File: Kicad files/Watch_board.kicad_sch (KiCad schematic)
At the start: 60 parts, among them J1 USB_C_Receptacle_USB2.0, J2 MOT1, J3 MOT2, Q1 BC846, SW2 BTN_L, SW3 BTN_R, U1 LTC3531, U2 MAX1811, U3 BMP280, U4 DS3231MZ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

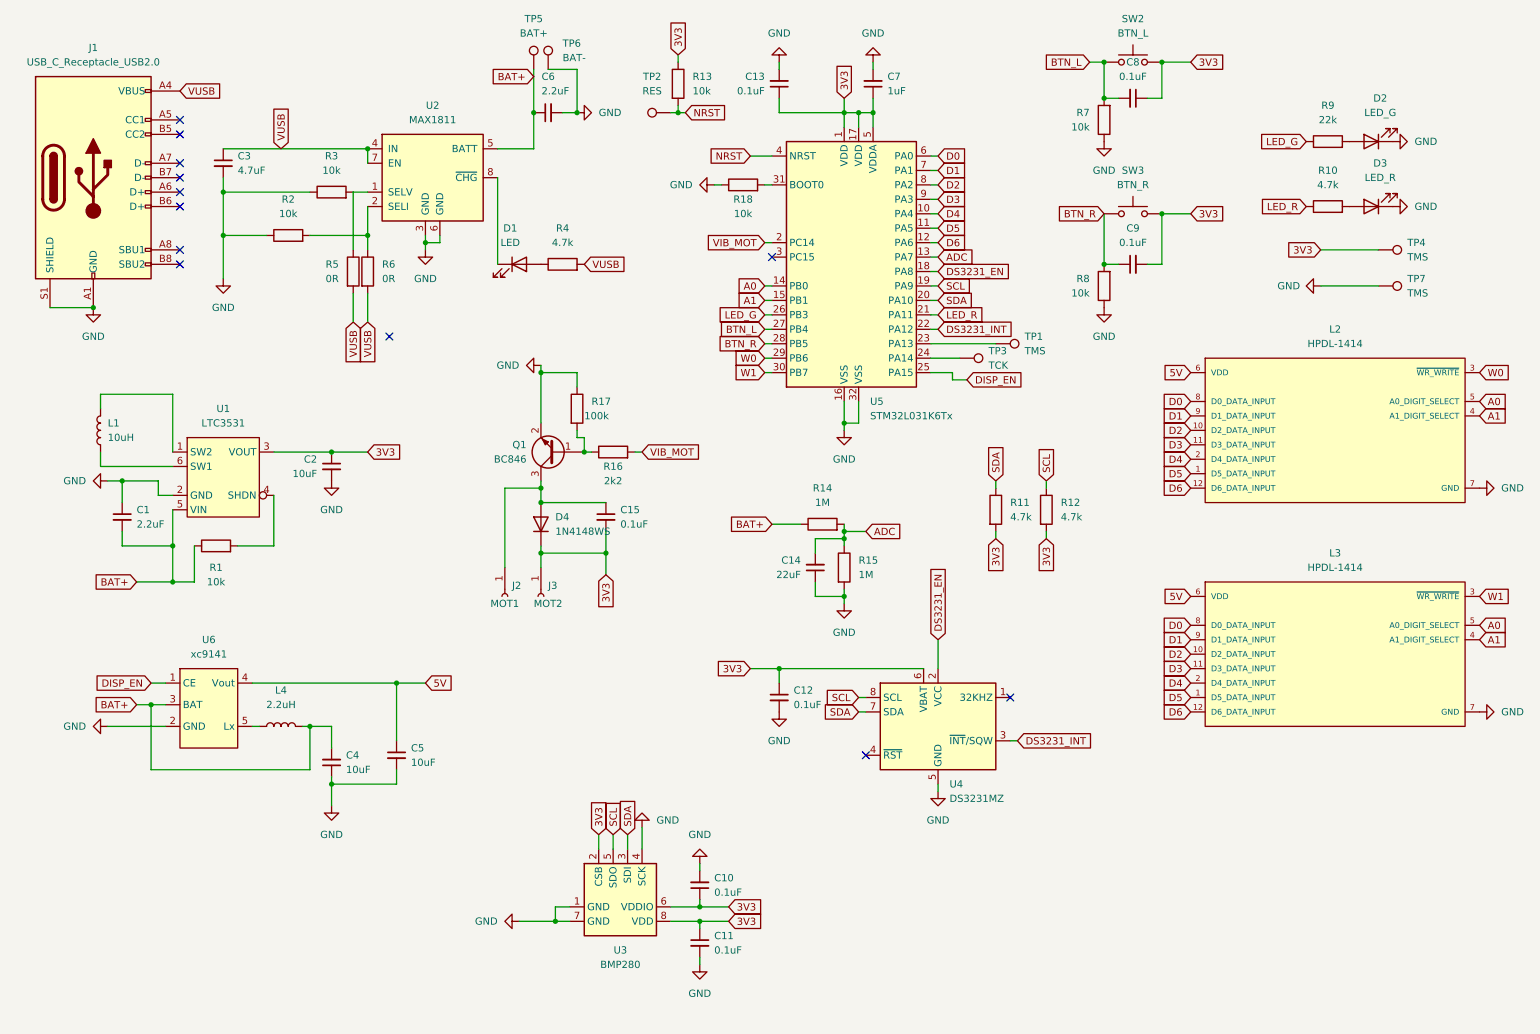
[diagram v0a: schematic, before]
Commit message: updated to HCMS-2904 (WIP)
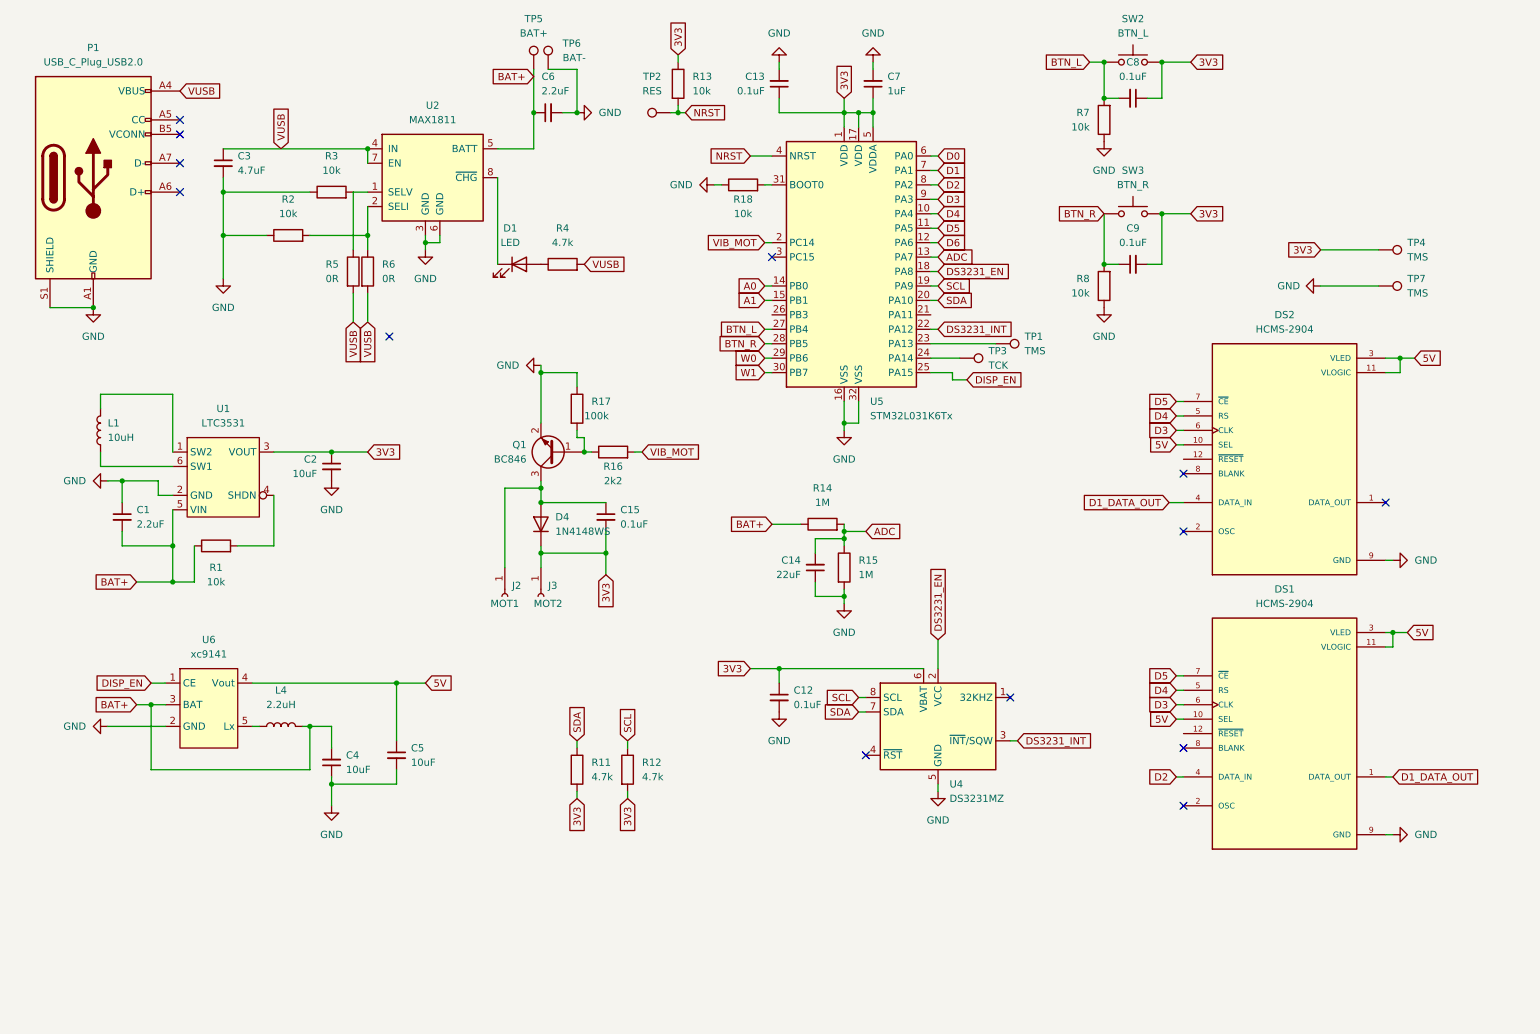
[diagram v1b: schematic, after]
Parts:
- removed C10, C11: 0.1uF, Capacitor_SMD:C_0603_1608Metric_Pad1.08x0.95mm_HandSolder, symbol Device:C_Small
- removed D2: LED_G, LED_SMD:LED_1206_3216Metric_Pad1.42x1.75mm_HandSolder, symbol Device:LED
- removed D3: LED_R, LED_SMD:LED_1206_3216Metric_Pad1.42x1.75mm_HandSolder, symbol Device:LED
- removed J1: USB_C_Receptacle_USB2.0, USB-C-Connectors:TYPE-C-31-M-17_handsolder, symbol Connector:USB_C_Receptacle_USB2.0
- removed L2, L3: HPDL-1414, eec:Broadcom-HPDL-1414-0, symbol eec:HPDL-1414
- removed R10: 4.7k, Resistor_SMD:R_0603_1608Metric_Pad0.98x0.95mm_HandSolder, symbol Device:R
- removed R9: 22k, Resistor_SMD:R_0603_1608Metric_Pad0.98x0.95mm_HandSolder, symbol Device:R
- removed U3: BMP280, Package_LGA:Bosch_LGA-8_2x2.5mm_P0.65mm_ClockwisePinNumbering, symbol Sensor_Pressure:BMP280
- added DS1, DS2: HCMS-2904, HCMS-290x:DIPS762W51P254L1778H508Q12, symbol HCMS-2901:HCMS-2901
- added P1: USB_C_Plug_USB2.0, USB-C-Connectors:TYPE-C-31-M-17_handsolder, symbol Connector:USB_C_Plug_USB2.0
- SW2, SW3: footprint Button_Switch_SMD:SW_Push_1P1T_NO_CK_KMR2 -> Button_Switch_SMD:SW_SPST_PTS810
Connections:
- net 5V: now also DS1.10 (SEL), DS1.11 (VLOGIC), DS1.3 (VLED), DS2.10 (SEL), DS2.11 (VLOGIC), DS2.3 (VLED)
- net D2: now also DS1.4 (DATA_IN)
- net D3: now also DS1.6 (CLK), DS2.6 (CLK)
- net D4: now also DS1.5 (RS), DS2.5 (RS)
- net D5: now also DS1.7 (~{CE}), DS2.7 (~{CE})
- net GND: now also DS1.9 (GND), DS2.9 (GND), P1.A1 (GND), P1.A12 (GND), P1.B1 (GND), P1.B12 (GND), P1.S1 (SHIELD)
- net VUSB: now also P1.A4 (VBUS), P1.A9 (VBUS), P1.B4 (VBUS), P1.B9 (VBUS)
- net LED_G: no longer names the net of U5.26 (PB3)
- net LED_R: no longer names the net of U5.21 (PA11)
- new net D1_DATA_OUT: DS1.1 (DATA_OUT), DS2.4 (DATA_IN)
- no-connect marks 12 -> 13
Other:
- moved on the sheet: R11, R12

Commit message: updated kicad schematics to add light sensor, updated code
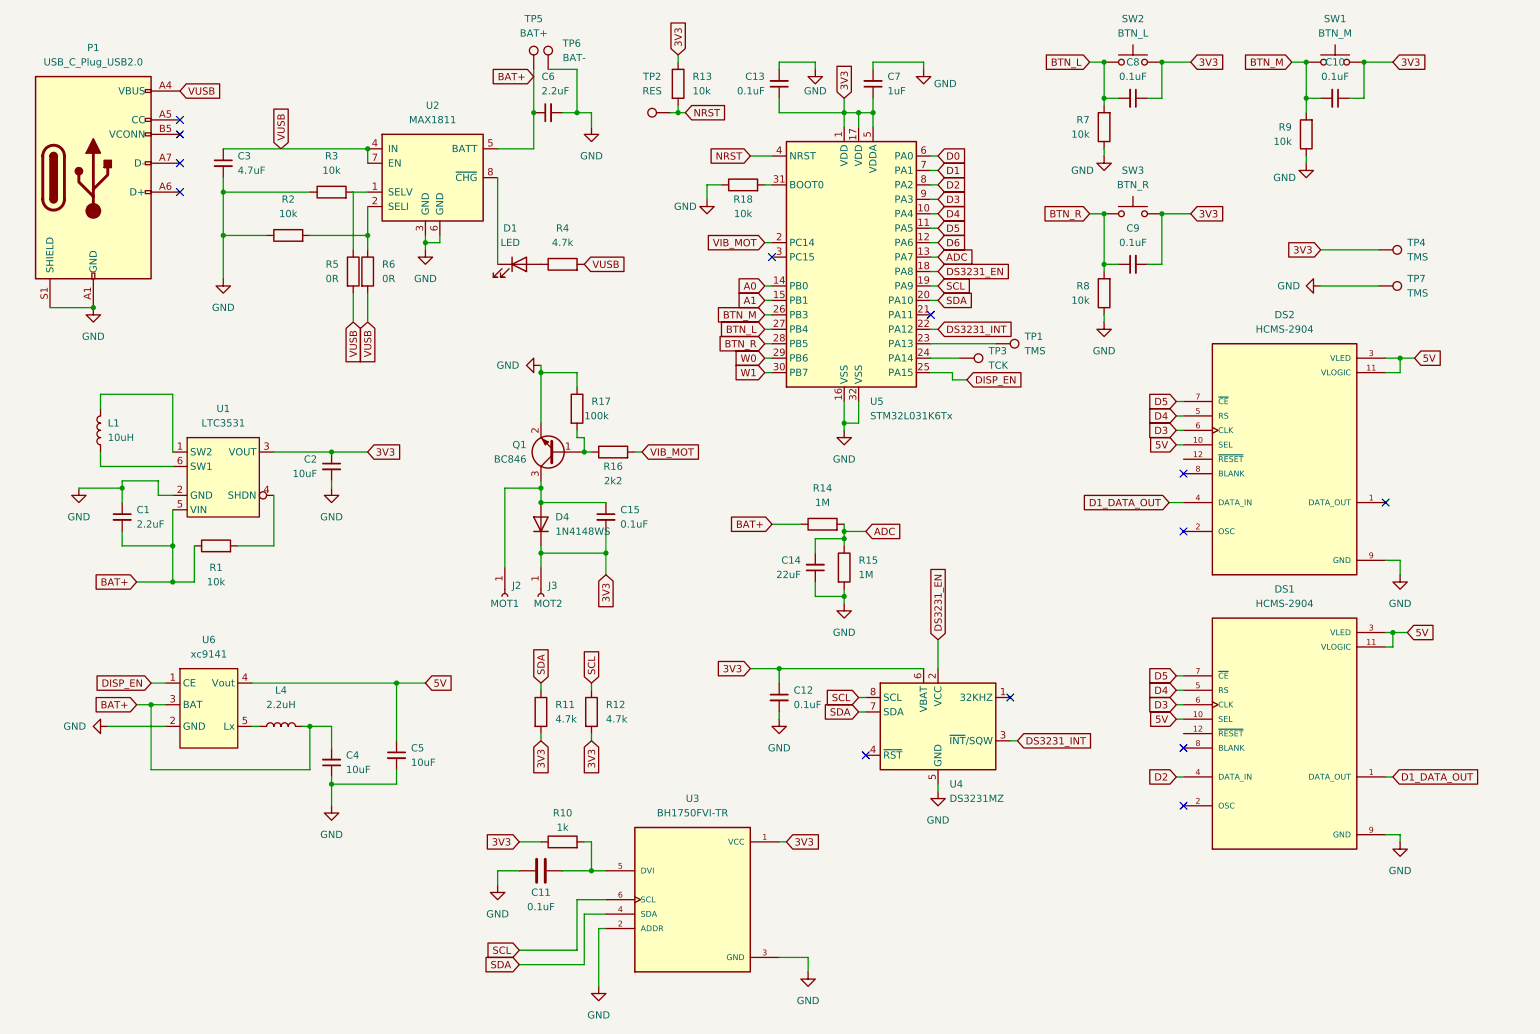
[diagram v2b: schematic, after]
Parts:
- added C10: 0.1uF, Capacitor_SMD:C_0603_1608Metric_Pad1.08x0.95mm_HandSolder, symbol Device:C_Small
- added C11: 0.1uF, Capacitor_SMD:C_0603_1608Metric_Pad1.08x0.95mm_HandSolder, symbol Device:C
- added R10: 1k, Resistor_SMD:R_0603_1608Metric_Pad0.98x0.95mm_HandSolder, symbol Device:R
- added R9: 10k, Resistor_SMD:R_0603_1608Metric_Pad0.98x0.95mm_HandSolder, symbol Device:R
- added SW1: BTN_M, Button_Switch_SMD:SW_SPST_PTS810, symbol Switch:SW_Push
- added U3: BH1750FVI-TR, BH1750FVI-TR:XDCR_BH1750FVI-TR, symbol BH1750FVI-TR:BH1750FVI-TR
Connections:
- net 3V3: now also C10.1, R10.1, SW1.2, U3.1 (VCC)
- net GND: now also C11.1, R9.1, U3.2 (ADDR), U3.3 (GND)
- net SCL: now also U3.6 (SCL)
- net SDA: now also U3.4 (SDA)
- net BTN_M: now reaches U5.26 (PB3)
- net BTN_M: now also C10.2, R9.2, SW1.1
- new net: C11.2, R10.2, U3.5 (DVI)
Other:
- moved on the sheet: R11, R12, R7, R8

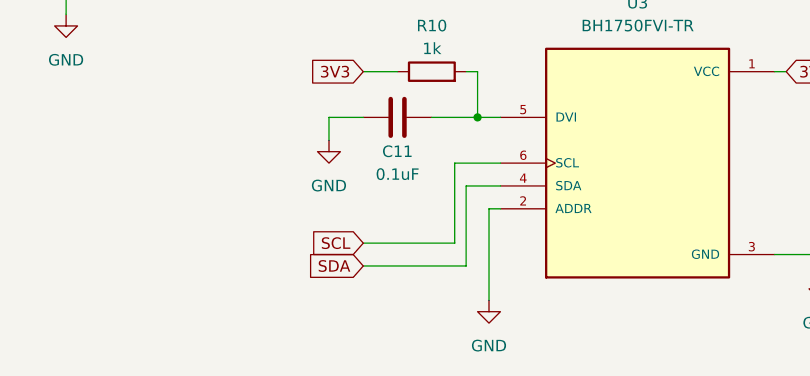
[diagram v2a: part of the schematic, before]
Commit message: added code for bh1750 light sensor
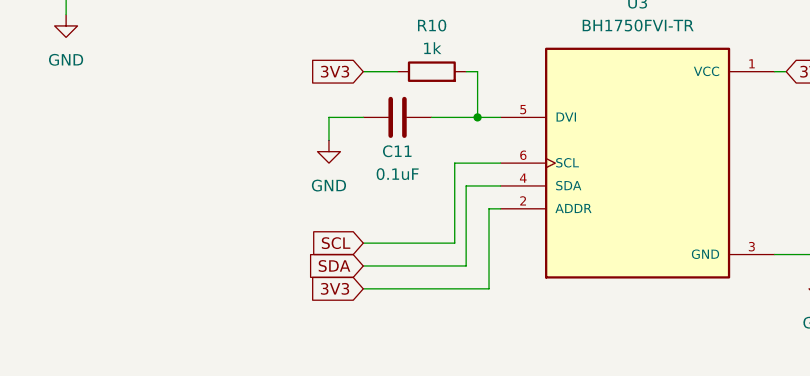
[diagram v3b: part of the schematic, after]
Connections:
- net 3V3: now also U3.2 (ADDR)
- net GND: no longer U3.2 (ADDR)
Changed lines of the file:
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@@
     (stroke (width 0) (type default))
   )
-  (wire (pts (xy 115.57 175.26) (xy 115.57 185.42))
+  (wire (pts (xy 115.57 175.26) (xy 115.57 184.15))
     (stroke (width 0) (type default))
   )
@@
     (stroke (width 0) (type default))
   )
+  (wire (pts (xy 101.6 184.15) (xy 115.57 184.15))
+    (stroke (width 0) (type default))
+  )
   (wire (pts (xy 256.54 160.02) (xy 256.54 158.75))
     (stroke (width 0) (type default))
@@
     (effects (font (size 1.27 1.27)) (justify right))
     (property "Intersheetrefs" "${INTERSHEET_REFS}" (at 116.7606 118.9507 90)
+      (effects (font (size 1.27 1.27)) (justify right) hide)
+    )
+  )
+  (global_label "3V3" (shape input) (at 101.6 184.15 180) (fields_autoplaced)
+    (effects (font (size 1.27 1.27)) (justify right))
+    (property "Intersheetrefs" "${INTERSHEET_REFS}" (at 95.1072 184.15 0)
       (effects (font (size 1.27 1.27)) (justify right) hide)
     )
@@
         )
       )
-    )
-  )
-  (symbol (lib_name "GND_1") (lib_id "power:GND") (at 115.57 185.42 0) (unit 1)
-    (in_bom yes) (on_board yes) (dnp no) (fields_autoplaced)
-    (property "Reference" "#PWR012" (at 115.57 191.77 0)
-      (effects (font (size 1.27 1.27)) hide)
-    )
-    (property "Value" "GND" (at 115.57 190.5 0)
-      (effects (font (size 1.27 1.27)))
-    )
-    (property "Footprint" "" (at 115.57 185.42 0)
-      (effects (font (size 1.27 1.27)) hide)
-    )
-    (property "Datasheet" "" (at 115.57 185.42 0)
-      (effects (font (size 1.27 1.27)) hide)
-    )
-    (pin "1")
-    (instances
-      (project "Watch_board"
-        (path "/e63e39d7-6ac0-4ffd-8aa3-1841a4541b55"
-          (reference "#PWR012") (unit 1)
-        )
-      )
